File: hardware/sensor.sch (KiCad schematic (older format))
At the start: 27 parts, among them J1 Conn_01x04, J2 Conn_01x04, J3 Conn_01x04, J4 Conn_01x04, J5 Conn_01x06, J6 Conn_01x06, J7 Conn_01x06, J8 Conn_01x06, U1 AP2112K-3.3TRG1, U2 ESP32-WROOM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

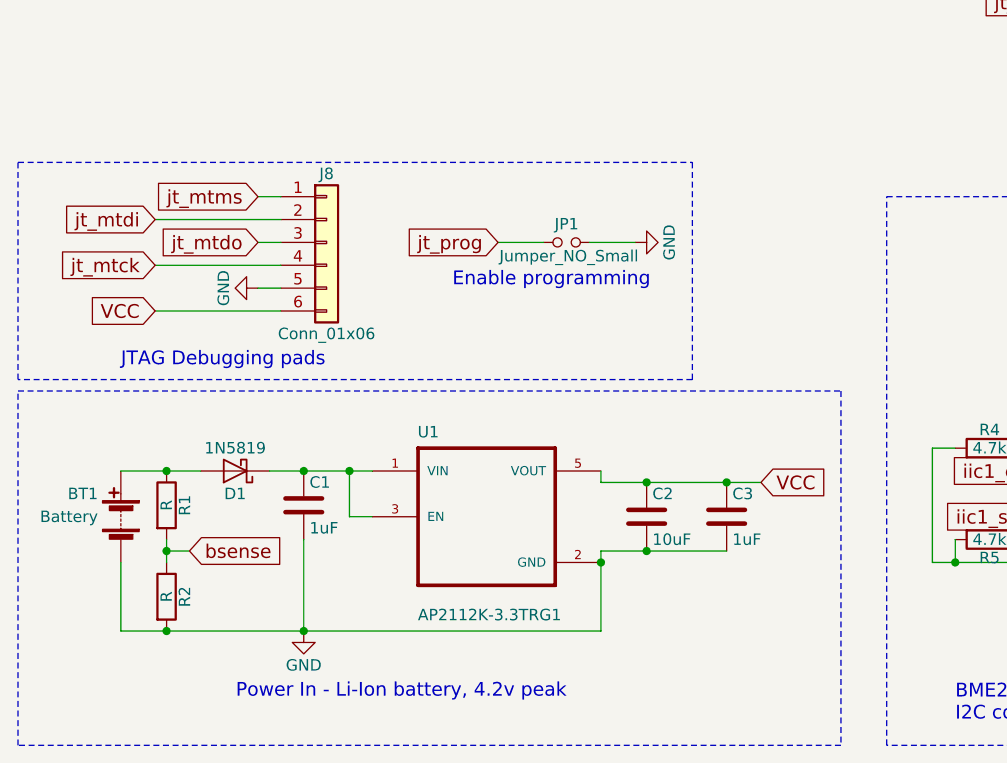
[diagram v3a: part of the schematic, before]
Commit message: Additional tweaks
Update footprints for SPI & I2C expansion
Set resistor values for battery voltage divider
Series resistors for JTAG
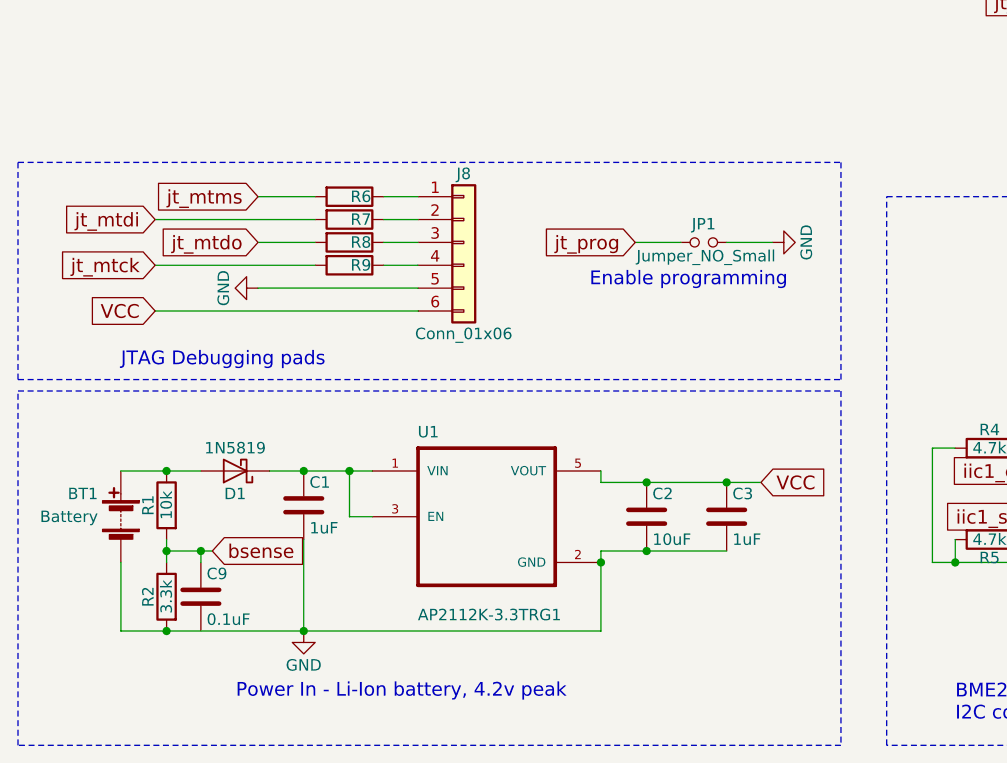
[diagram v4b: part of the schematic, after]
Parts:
- added C9: 0.1uF, Capacitors_SMD:C_1206, symbol C
- added R6, R7, R8, R9: 100, Resistors_SMD:R_1206, symbol R
- J1, J2, J3, J4: footprint Pin_Headers:Pin_Header_Straight_1x04_Pitch1.00mm -> Pin_Headers:Pin_Header_Straight_1x04_Pitch2.54mm
- J5, J6, J7, J8: footprint Pin_Headers:Pin_Header_Straight_1x06_Pitch1.00mm -> Pin_Headers:Pin_Header_Straight_1x06_Pitch2.54mm
- JP1: footprint Capacitors_SMD:C_0402 -> Pin_Headers:Pin_Header_Straight_1x02_Pitch2.54mm
- R1: value R -> 10k
- R2: value R -> 3.3k
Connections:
- net bsense: now also C9.1
- net jt_mtck: now also R9.2; no longer J8.4 (Pin_4)
- net jt_mtdi: now also R7.2; no longer J8.2 (Pin_2)
- net jt_mtdo: now also R8.2; no longer J8.3 (Pin_3)
- net jt_mtms: now also R6.2; no longer J8.1 (Pin_1)
- new net: J8.1 (Pin_1), R6.1
- new net: J8.2 (Pin_2), R7.1
- new net: J8.3 (Pin_3), R8.1
- new net: J8.4 (Pin_4), R9.1
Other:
- moved on the sheet: J8, JP1
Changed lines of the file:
@@
 P 1250 7050
 F 0 "R2" V 1330 7050 50  0000 C CNN
-F 1 "R" V 1250 7050 50  0000 C CNN
+F 1 "3.3k" V 1250 7050 50  0000 C CNN
 F 2 "Resistors_SMD:R_1206" V 1180 7050 50  0001 C CNN
 F 3 "" H 1250 7050 50  0001 C CNN
 	1    1250 7050
-	1    0    0    -1
+	-1   0    0    -1
 $EndComp
 $Comp
@@
 P 1250 6650
 F 0 "R1" V 1330 6650 50  0000 C CNN
-F 1 "R" V 1250 6650 50  0000 C CNN
+F 1 "10k" V 1250 6650 50  0000 C CNN
 F 2 "Resistors_SMD:R_1206" V 1180 6650 50  0001 C CNN
 F 3 "" H 1250 6650 50  0001 C CNN
 	1    1250 6650
-	1    0    0    -1
+	-1   0    0    -1
 $EndComp
 $Comp
@@
 Text GLabel 3850 6550 2    60   Input ~ 0
 VCC
-Text GLabel 1350 6850 2    60   Input ~ 0
+Text GLabel 1450 6850 2    60   Input ~ 0
 bsense
 Text Notes 3000 7500 2    60   ~ 0
@@
 F 0 "J1" H 7700 6050 50  0000 C CNN
 F 1 "Conn_01x04" H 7700 5550 50  0000 C CNN
-F 2 "Pin_Headers:Pin_Header_Straight_1x04_Pitch1.00mm" H 7700 5850 50  0001 C CNN
+F 2 "Pin_Headers:Pin_Header_Straight_1x04_Pitch2.54mm" H 7700 5850 50  0001 C CNN
 F 3 "" H 7700 5850 50  0001 C CNN
 	1    7700 5850
@@
 F 0 "J2" H 8650 6050 50  0000 C CNN
 F 1 "Conn_01x04" H 8650 5550 50  0000 C CNN
-F 2 "Pin_Headers:Pin_Header_Straight_1x04_Pitch1.00mm" H 8650 5850 50  0001 C CNN
+F 2 "Pin_Headers:Pin_Header_Straight_1x04_Pitch2.54mm" H 8650 5850 50  0001 C CNN
 F 3 "" H 8650 5850 50  0001 C CNN
 	1    8650 5850
@@
 F 0 "J3" H 9550 6050 50  0000 C CNN
 F 1 "Conn_01x04" H 9550 5550 50  0000 C CNN
-F 2 "Pin_Headers:Pin_Header_Straight_1x04_Pitch1.00mm" H 9550 5850 50  0001 C CNN
+F 2 "Pin_Headers:Pin_Header_Straight_1x04_Pitch2.54mm" H 9550 5850 50  0001 C CNN
 F 3 "" H 9550 5850 50  0001 C CNN
 	1    9550 5850
@@
 F 0 "J4" H 10550 6050 50  0000 C CNN
 F 1 "Conn_01x04" H 10550 5550 50  0000 C CNN
-F 2 "Pin_Headers:Pin_Header_Straight_1x04_Pitch1.00mm" H 10550 5850 50  0001 C CNN
+F 2 "Pin_Headers:Pin_Header_Straight_1x04_Pitch2.54mm" H 10550 5850 50  0001 C CNN
 F 3 "" H 10550 5850 50  0001 C CNN
 	1    10550 5850
@@
 F 0 "J6" H 9300 4750 50  0000 C CNN
 F 1 "Conn_01x06" H 9300 4050 50  0000 C CNN
-F 2 "Pin_Headers:Pin_Header_Straight_1x06_Pitch1.00mm" H 9300 4450 50  0001 C CNN
+F 2 "Pin_Headers:Pin_Header_Straight_1x06_Pitch2.54mm" H 9300 4450 50  0001 C CNN
 F 3 "" H 9300 4450 50  0001 C CNN
 	1    9300 4450
@@
 Connection ~ 1250 6850
 Wire Wire Line
-	1350 6850 1250 6850
+	1450 6850 1250 6850
 Wire Wire Line
 	1250 6800 1250 6900
@@
 F 0 "J5" H 8200 4750 50  0000 C CNN
 F 1 "Conn_01x06" H 8200 4050 50  0000 C CNN
-F 2 "Pin_Headers:Pin_Header_Straight_1x06_Pitch1.00mm" H 8200 4450 50  0001 C CNN
+F 2 "Pin_Headers:Pin_Header_Straight_1x06_Pitch2.54mm" H 8200 4450 50  0001 C CNN
 F 3 "" H 8200 4450 50  0001 C CNN
 	1    8200 4450
@@
 F 0 "J7" H 10350 4750 50  0000 C CNN
 F 1 "Conn_01x06" H 10350 4050 50  0000 C CNN
-F 2 "Pin_Headers:Pin_Header_Straight_1x06_Pitch1.00mm" H 10350 4450 50  0001 C CNN
+F 2 "Pin_Headers:Pin_Header_Straight_1x06_Pitch2.54mm" H 10350 4450 50  0001 C CNN
 F 3 "" H 10350 4450 50  0001 C CNN
 	1    10350 4450
@@
 L Conn_01x06 J8
 U 1 1 5B3C465C
-P 1950 5500
-F 0 "J8" H 1950 5800 50  0000 C CNN
-F 1 "Conn_01x06" H 1950 5100 50  0000 C CNN
-F 2 "Pin_Headers:Pin_Header_Straight_1x06_Pitch1.00mm" H 1950 5500 50  0001 C CNN
-F 3 "" H 1950 5500 50  0001 C CNN
-	1    1950 5500
+P 2550 5500
+F 0 "J8" H 2550 5800 50  0000 C CNN
+F 1 "Conn_01x06" H 2550 5100 50  0000 C CNN
+F 2 "Pin_Headers:Pin_Header_Straight_1x06_Pitch2.54mm" H 2550 5500 50  0001 C CNN
+F 3 "" H 2550 5500 50  0001 C CNN
+	1    2550 5500
 	1    0    0    -1
 $EndComp
@@
 VCC
 Wire Wire Line
-	1650 5300 1750 5300
-Wire Wire Line
-	1750 5400 1200 5400
-Wire Wire Line
-	1200 5600 1750 5600
-Wire Wire Line
-	1750 5500 1650 5500
-Wire Wire Line
-	1650 5700 1750 5700
-Wire Wire Line
-	1750 5800 1200 5800
-Text GLabel 2700 5500 0    60   Input ~ 0
+	1650 5300 1900 5300
+Wire Wire Line
+	1900 5400 1200 5400
+Wire Wire Line
+	1200 5600 1900 5600
+Wire Wire Line
+	1900 5500 1650 5500
+Wire Wire Line
+	1650 5700 2350 5700
+Wire Wire Line
+	2350 5800 1200 5800
+Text GLabel 3300 5500 0    60   Input ~ 0
 jt_prog
 $Comp
 L GND #PWR019
 U 1 1 5B3C6E69
-P 3300 5500
-F 0 "#PWR019" H 3300 5250 50  0001 C CNN
-F 1 "GND" H 3300 5350 50  0000 C CNN
-F 2 "" H 3300 5500 50  0001 C CNN
-F 3 "" H 3300 5500 50  0001 C CNN
-	1    3300 5500
+P 3900 5500
+F 0 "#PWR019" H 3900 5250 50  0001 C CNN
+F 1 "GND" H 3900 5350 50  0000 C CNN
+F 2 "" H 3900 5500 50  0001 C CNN
+F 3 "" H 3900 5500 50  0001 C CNN
+	1    3900 5500
 	0    -1   -1   0
 $EndComp
@@
 L Jumper_NO_Small JP1
 U 1 1 5B3C6EFA
-P 3000 5500
-F 0 "JP1" H 3000 5580 50  0000 C CNN
-F 1 "Jumper_NO_Small" H 3010 5440 50  0000 C CNN
-F 2 "Capacitors_SMD:C_0402" H 3000 5500 50  0001 C CNN
-F 3 "" H 3000 5500 50  0001 C CNN
-	1    3000 5500
-	1    0    0    -1
-$EndComp
-Wire Wire Line
-	2700 5500 2900 5500
-Wire Wire Line
-	3100 5500 3300 5500
-Text Notes 2500 5700 0    60   ~ 0
+P 3600 5500
+F 0 "JP1" H 3600 5580 50  0000 C CNN
+F 1 "Jumper_NO_Small" H 3610 5440 50  0000 C CNN
+F 2 "Pin_Headers:Pin_Header_Straight_1x02_Pitch2.54mm" H 3600 5500 50  0001 C CNN
+F 3 "" H 3600 5500 50  0001 C CNN
+	1    3600 5500
+	1    0    0    -1
+$EndComp
+Wire Wire Line
+	3300 5500 3500 5500
+Wire Wire Line
+	3700 5500 3900 5500
+Text Notes 3100 5700 0    60   ~ 0
 Enable programming
 Text Notes 1050 6050 0    60   ~ 0
@@
 	600  6100 600  5150
 Wire Notes Line
-	600  5150 3550 5150
-Wire Notes Line
-	3550 5150 3550 6100
-Wire Notes Line
-	3550 6100 600  6100
+	600  5150 4200 5150
+Wire Notes Line
+	600  6100 4200 6100
 NoConn ~ 5950 2300
 NoConn ~ 5950 2400
@@
 Text Notes 2300 1700 0    60   ~ 0
 Chip powerup RC timer
+$Comp
+L R R6
+U 1 1 5B3CD9E4
+P 2050 5300
+F 0 "R6" V 2050 5350 50  0000 C CNN
+F 1 "100" V 2050 5250 50  0001 C CNN
+F 2 "Resistors_SMD:R_1206" V 1980 5300 50  0001 C CNN
+F 3 "" H 2050 5300 50  0001 C CNN
+	1    2050 5300
+	0    1    1    0
+$EndComp
+$Comp
+L R R7
+U 1 1 5B3CDE47
+P 2050 5400
+F 0 "R7" V 2050 5450 50  0000 C CNN
+F 1 "100" V 2050 5350 50  0001 C CNN
+F 2 "Resistors_SMD:R_1206" V 1980 5400 50  0001 C CNN
+F 3 "" H 2050 5400 50  0001 C CNN
+	1    2050 5400
+	0    1    1    0
+$EndComp
+$Comp
+L R R8
+U 1 1 5B3CDECB
+P 2050 5500
+F 0 "R8" V 2050 5550 50  0000 C CNN
+F 1 "100" V 2050 5450 50  0001 C CNN
+F 2 "Resistors_SMD:R_1206" V 1980 5500 50  0001 C CNN
+F 3 "" H 2050 5500 50  0001 C CNN
+	1    2050 5500
+	0    1    1    0
+$EndComp
+$Comp
+L R R9
+U 1 1 5B3CDF35
+P 2050 5600
+F 0 "R9" V 2050 5650 50  0000 C CNN
+F 1 "100" V 2050 5550 50  0001 C CNN
+F 2 "Resistors_SMD:R_1206" V 1980 5600 50  0001 C CNN
+F 3 "" H 2050 5600 50  0001 C CNN
+	1    2050 5600
+	0    1    1    0
+$EndComp
+Wire Wire Line
+	2200 5600 2350 5600
+Wire Wire Line
+	2350 5500 2200 5500
+Wire Wire Line
+	2200 5400 2350 5400
+Wire Wire Line
+	2200 5300 2350 5300
+$Comp
+L C C9
+U 1 1 5B3CE78D
+P 1400 7050
+F 0 "C9" H 1425 7150 50  0000 L CNN
+F 1 "0.1uF" H 1425 6950 50  0000 L CNN
+F 2 "Capacitors_SMD:C_1206" H 1438 6900 50  0001 C CNN
+F 3 "" H 1400 7050 50  0001 C CNN
+	1    1400 7050
+	1    0    0    -1
+$EndComp
+Wire Wire Line
+	1400 6900 1400 6850
+Connection ~ 1400 6850
+Wire Notes Line
+	4200 6100 4200 5150
 $EndSCHEMATC

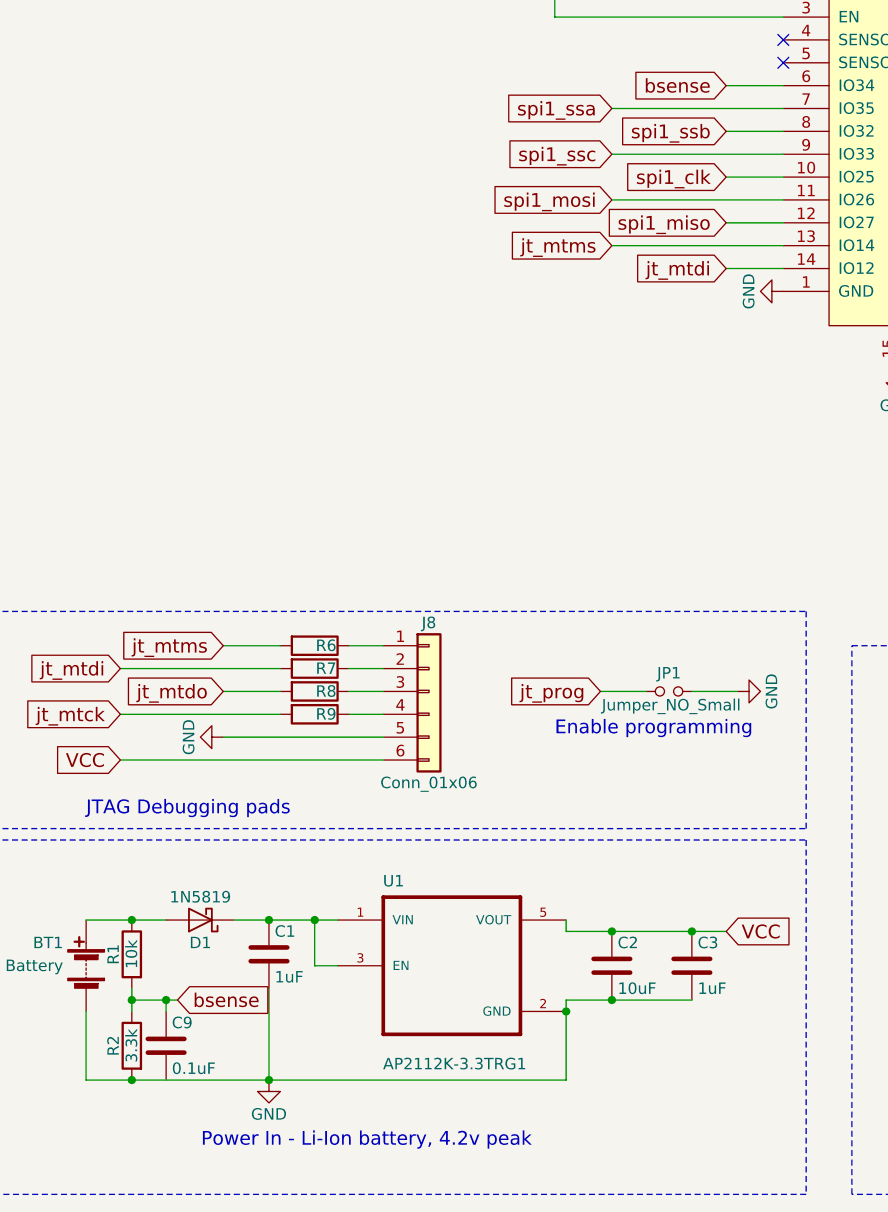
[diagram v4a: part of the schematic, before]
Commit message: Additional fixes, Place & route board
* Add junction on C9 to GND
* Swap SPI pins for cleaner routing
* Finish initial routing of board

TODO: Finish silkscreen layout
* Reference labels
* Page labels
* Board version markings
* Art
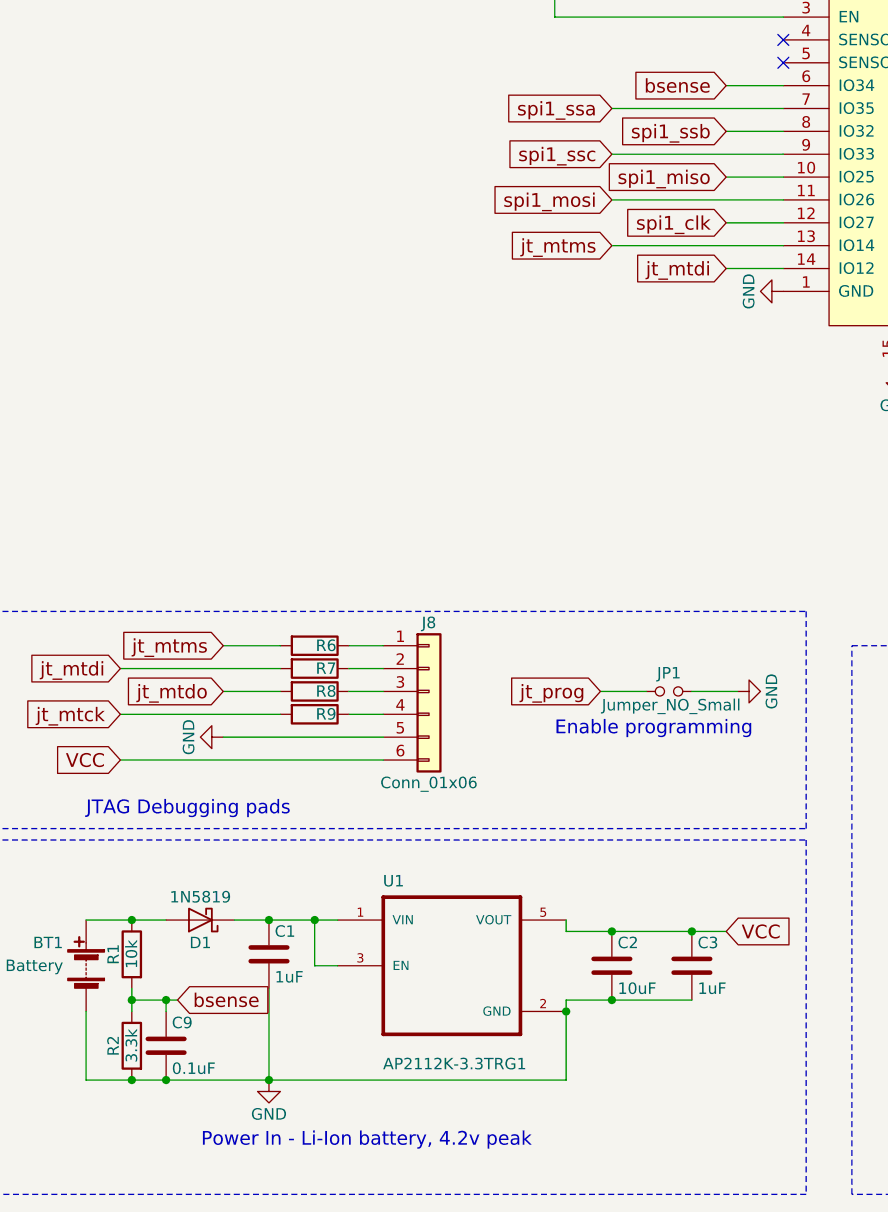
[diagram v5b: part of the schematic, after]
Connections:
- net GND: now also C9.2
- net spi1_clk: now also U2.12 (IO27); no longer U2.10 (IO25)
- net spi1_miso: now also U2.10 (IO25); no longer U2.12 (IO27)
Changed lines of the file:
@@
 NoConn ~ 5200 4100
 NoConn ~ 5300 4100
-Text GLabel 3850 3250 0    60   Input ~ 0
+Text GLabel 3850 3450 0    60   Input ~ 0
 spi1_clk
 Text GLabel 3350 3350 0    60   Input ~ 0
 spi1_mosi
-Text GLabel 3850 3450 0    60   Input ~ 0
+Text GLabel 3850 3250 0    60   Input ~ 0
 spi1_miso
 Text GLabel 3350 2950 0    60   Input ~ 0
@@
 Wire Notes Line
 	4200 6100 4200 5150
+Connection ~ 1400 7200
 $EndSCHEMATC
